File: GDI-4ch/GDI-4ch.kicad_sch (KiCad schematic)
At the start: 312 parts, among them J1 Conn_02x02_Odd_Even, J2 FTSH-107-01-F-DV-K, J3 TC2030, J4 Conn_01x06, J5 Conn_01x04, P1 368255-2, P18 Pad, P19 Pad, P2 Pad, P20 Pad, P3 Pad, P32 Pad, P36 Pad, P4 Pad, P5 Pad, Q1 BUK9230-100B, Q10 BUK9230-100B, Q11 BUK9230-100B, Q12 BUK9230-100B, Q13 AOD4185, Q14 VND14NV04TR-E, Q15 VND14NV04TR-E, Q16 BUK9230-100B, Q2 BUK9230-100B, Q3 BUK9230-100B, Q4 BUK9230-100B, Q5 BUK9230-100B, Q6 BUK9230-100B, Q7 BUK9230-100B, Q8 BUK9230-100B, Q9 BUK9230-100B, U1 MC33816, U2 TJA1051T-3, U3 LM78M05_TO252, U4 74HC14PW,118, U5 XC6206P332MR, U6 MCP6004, U7 GD32F103CBT6, U8 74HC14PW,118, Y1 8MHz, Y2 1MHz

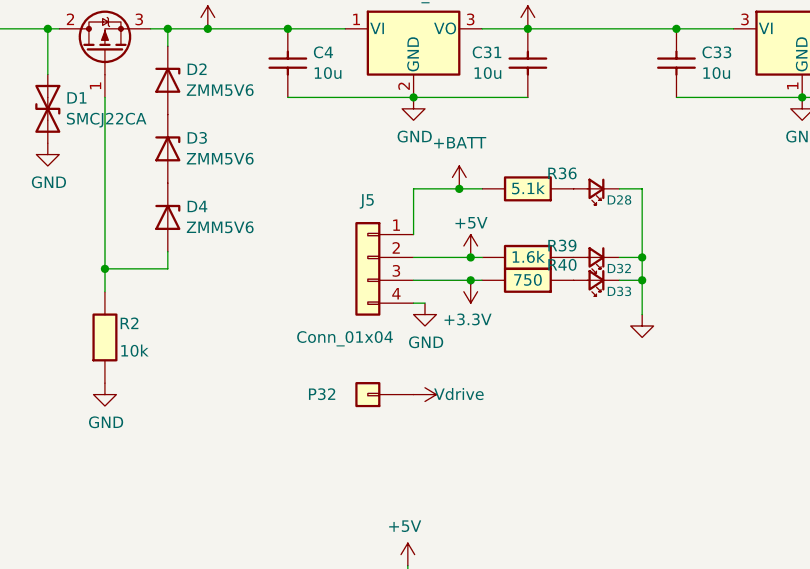
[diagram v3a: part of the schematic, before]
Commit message: 6-pin power connector
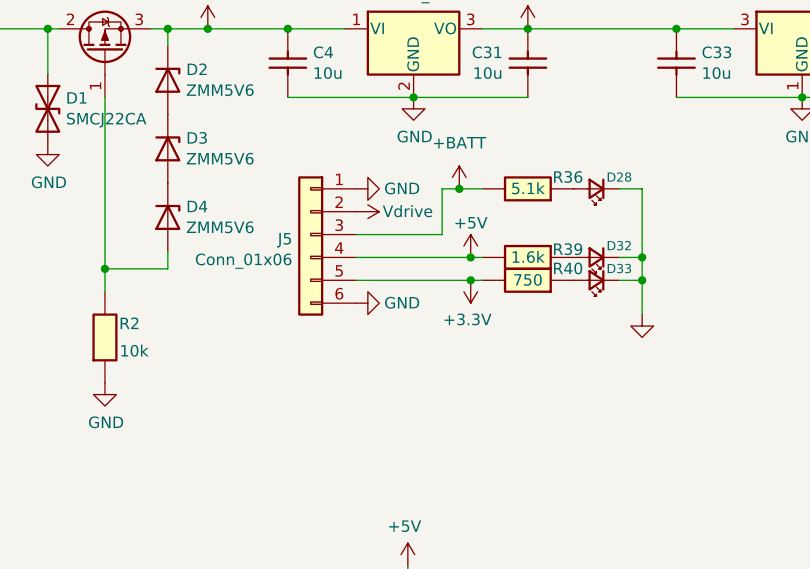
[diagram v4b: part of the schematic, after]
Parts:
- removed J5: Conn_01x04, Connector_PinHeader_2.54mm:PinHeader_1x04_P2.54mm_Vertical, symbol Connector_Generic:Conn_01x04
- removed P32: Pad, hellen-one-common:PAD-TH, symbol hellen-one-common:Pad
- added J5: Conn_01x06, Connector_PinHeader_2.54mm:PinHeader_1x06_P2.54mm_Vertical, symbol Connector_Generic:Conn_01x06
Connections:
- net +3.3V: now also J5.5 (Pin_5)
- net +5V: now also J5.4 (Pin_4)
- net +BATT: now also J5.3 (Pin_3)
- net GND: now also J5.1 (Pin_1), J5.6 (Pin_6)
- net Vdrive: now also J5.2 (Pin_2)
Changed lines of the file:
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@@
     (stroke (width 0) (type default))
   )
+  (wire (pts (xy 113.03 46.99) (xy 122.555 46.99))
+    (stroke (width 0) (type default))
+  )
   (wire (pts (xy 92.075 48.895) (xy 92.075 50.8))
     (stroke (width 0) (type default))
@@
     (stroke (width 0) (type default))
   )
-  (wire (pts (xy 119.38 41.91) (xy 119.38 46.99))
+  (wire (pts (xy 122.555 41.91) (xy 122.555 46.99))
     (stroke (width 0) (type default))
   )
@@
     (stroke (width 0) (type default))
   )
-  (wire (pts (xy 119.38 54.61) (xy 120.65 54.61))
-    (stroke (width 0) (type default))
-  )
   (wire (pts (xy 398.78 104.14) (xy 411.48 104.14))
     (stroke (width 0) (type default))
@@
     (stroke (width 0) (type default))
   )
-  (wire (pts (xy 119.38 49.53) (xy 125.73 49.53))
+  (wire (pts (xy 113.03 49.53) (xy 125.73 49.53))
     (stroke (width 0) (type default))
   )
@@
     (stroke (width 0) (type default))
   )
-  (wire (pts (xy 119.38 41.91) (xy 124.46 41.91))
+  (wire (pts (xy 122.555 41.91) (xy 124.46 41.91))
     (stroke (width 0) (type default))
   )
@@
     (stroke (width 0) (type solid))
   )
-  (wire (pts (xy 119.38 52.07) (xy 125.73 52.07))
+  (wire (pts (xy 113.03 52.07) (xy 125.73 52.07))
     (stroke (width 0) (type default))
   )
@@
   (symbol (lib_id "Device:LED_Small") (at 139.7 49.53 180) (unit 1)
     (in_bom yes) (on_board yes) (dnp no)
-    (property "Reference" "D32" (at 142.24 50.8 0)
+    (property "Reference" "D32" (at 142.24 48.26 0)
       (effects (font (size 1.016 1.016)))
     )
@@
   (symbol (lib_id "Device:LED_Small") (at 139.7 41.91 180) (unit 1)
     (in_bom yes) (on_board yes) (dnp no)
-    (property "Reference" "D28" (at 142.24 43.18 0)
+    (property "Reference" "D28" (at 142.24 40.64 0)
       (effects (font (size 1.016 1.016)))
     )
@@
   (symbol (lib_id "Device:LED_Small") (at 139.7 52.07 180) (unit 1)
     (in_bom yes) (on_board yes) (dnp no)
-    (property "Reference" "D33" (at 142.24 53.34 0)
+    (property "Reference" "D33" (at 142.24 50.8 0)
       (effects (font (size 1.016 1.016)))
     )
@@
   (symbol (lib_id "hellen-one-common:Res") (at 137.16 49.53 180) (unit 1)
     (in_bom yes) (on_board yes) (dnp no)
-    (property "Reference" "R39" (at 135.89 48.26 0)
+    (property "Reference" "R39" (at 136.525 48.6602 0)
       (effects (font (size 1.27 1.27)))
     )
@@
     )
   )
-  (symbol (lib_id "hellen-one-common:Pad") (at 114.3 64.77 180) (unit 1)
-    (in_bom yes) (on_board yes) (dnp no)
-    (property "Reference" "P32" (at 109.22 64.77 0)
-      (effects (font (size 1.27 1.27)))
-    )
-    (property "Value" "Pad" (at 114.3 62.23 0)
-      (effects (font (size 1.27 1.27)) hide)
-    )
-    (property "Footprint" "hellen-one-common:PAD-TH" (at 114.3 60.96 0)
-      (effects (font (size 1.27 1.27)) hide)
-    )
-    (property "Datasheet" "~" (at 114.3 64.77 0)
-      (effects (font (size 1.27 1.27)) hide)
-    )
-    (pin "1")
-    (instances
-      (project "GDI-4ch"
-        (path "/03caada9-9e22-4e2d-9035-b15433dfbb17"
-          (reference "P32") (unit 1)
-        )
-      )
-    )
-  )
   (symbol (lib_id "hellen-one-common:Button_SPST") (at 340.995 16.51 0) (mirror y) (unit 1)
     (in_bom yes) (on_board yes) (dnp no)
@@
     )
   )
-  (symbol (lib_id "Connector_Generic:Conn_01x04") (at 114.3 49.53 0) (mirror y) (unit 1)
-    (in_bom yes) (on_board yes) (dnp no)
-    (property "Reference" "J5" (at 114.3 43.18 0)
-      (effects (font (size 1.27 1.27)))
-    )
-    (property "Value" "Conn_01x04" (at 111.76 58.42 0)
-      (effects (font (size 1.27 1.27)))
-    )
-    (property "Footprint" "Connector_PinHeader_2.54mm:PinHeader_1x04_P2.54mm_Vertical" (at 114.3 49.53 0)
-      (effects (font (size 1.27 1.27)) hide)
-    )
-    (property "Datasheet" "~" (at 114.3 49.53 0)
-      (effects (font (size 1.27 1.27)) hide)
-    )
-    (pin "1")
-    (pin "2")
-    (pin "3")
-    (pin "4")
-    (instances
-      (project "GDI-4ch"
-        (path "/03caada9-9e22-4e2d-9035-b15433dfbb17"
-          (reference "J5") (unit 1)
-        )
-      )
-    )
-  )
   (symbol (lib_id "power:+3.3V") (at 136.525 198.755 0) (unit 1)
     (in_bom yes) (on_board yes) (dnp no)
@@
     )
   )
+  (symbol (lib_id "power:GND") (at 113.03 41.91 90) (unit 1)
+    (in_bom yes) (on_board yes) (dnp no)
+    (property "Reference" "#PWR0150" (at 119.38 41.91 0)
+      (effects (font (size 1.27 1.27)) hide)
+    )
+    (property "Value" "GND" (at 118.11 41.91 90)
+      (effects (font (size 1.27 1.27)))
+    )
+    (property "Footprint" "" (at 113.03 41.91 0)
+      (effects (font (size 1.27 1.27)) hide)
+    )
+    (property "Datasheet" "" (at 113.03 41.91 0)
+      (effects (font (size 1.27 1.27)) hide)
+    )
+    (pin "1")
+    (instances
+      (project "GDI-4ch"
+        (path "/03caada9-9e22-4e2d-9035-b15433dfbb17"
+          (reference "#PWR0150") (unit 1)
+        )
+      )
+    )
+  )
   (symbol (lib_id "Device:R") (at 361.95 66.04 270) (unit 1)
     (in_bom yes) (on_board yes) (dnp no)
@@
     )
   )
-  (symbol (lib_id "power:Vdrive") (at 119.38 64.77 270) (unit 1)
+  (symbol (lib_id "power:Vdrive") (at 113.03 44.45 270) (unit 1)
     (in_bom yes) (on_board yes) (dnp no)
-    (property "Reference" "#PWR024" (at 115.57 59.69 0)
+    (property "Reference" "#PWR024" (at 109.22 39.37 0)
       (effects (font (size 1.27 1.27)) hide)
     )
-    (property "Value" "Vdrive" (at 124.46 64.77 90)
+    (property "Value" "Vdrive" (at 118.745 44.45 90)
       (effects (font (size 1.27 1.27)))
     )
-    (property "Footprint" "" (at 119.38 64.77 0)
+    (property "Footprint" "" (at 113.03 44.45 0)
       (effects (font (size 1.27 1.27)) hide)
     )
-    (property "Datasheet" "" (at 119.38 64.77 0)
+    (property "Datasheet" "" (at 113.03 44.45 0)
       (effects (font (size 1.27 1.27)) hide)
     )
@@
     )
   )
+  (symbol (lib_id "Connector_Generic:Conn_01x06") (at 107.95 46.99 0) (mirror y) (unit 1)
+    (in_bom yes) (on_board yes) (dnp no)
+    (property "Reference" "J5" (at 105.9179 47.4991 0)
+      (effects (font (size 1.27 1.27)) (justify left))
+    )
+    (property "Value" "Conn_01x06" (at 105.9179 49.7978 0)
+      (effects (font (size 1.27 1.27)) (justify left))
+    )
+    (property "Footprint" "Connector_PinHeader_2.54mm:PinHeader_1x06_P2.54mm_Vertical" (at 107.95 46.99 0)
+      (effects (font (size 1.27 1.27)) hide)
+    )
+    (property "Datasheet" "~" (at 107.95 46.99 0)
+      (effects (font (size 1.27 1.27)) hide)
+    )
+    (property "LCSC" "C5156615" (at 107.95 46.99 0)
+      (effects (font (size 1.524 1.524)) hide)
+    )
+    (pin "1")
+    (pin "2")
+    (pin "3")
+    (pin "4")
+    (pin "5")
+    (pin "6")
+    (instances
+      (project "GDI-4ch"
+        (path "/03caada9-9e22-4e2d-9035-b15433dfbb17"
+          (reference "J5") (unit 1)
+        )
+      )
+    )
+  )
   (symbol (lib_id "hellen-one-common:Cap") (at 167.005 202.565 270) (mirror x) (unit 1)
     (in_bom yes) (on_board yes) (dnp no)
@@
     )
   )
-  (symbol (lib_id "power:GND") (at 120.65 54.61 0) (unit 1)
-    (in_bom yes) (on_board yes) (dnp no)
-    (property "Reference" "#PWR0142" (at 120.65 60.96 0)
-      (effects (font (size 1.27 1.27)) hide)
-    )
-    (property "Value" "GND" (at 120.777 59.0042 0)
-      (effects (font (size 1.27 1.27)))
-    )
-    (property "Footprint" "" (at 120.65 54.61 0)
-      (effects (font (size 1.27 1.27)) hide)
-    )
-    (property "Datasheet" "" (at 120.65 54.61 0)
-      (effects (font (size 1.27 1.27)) hide)
-    )
-    (pin "1")
-    (instances
-      (project "GDI-4ch"
-        (path "/03caada9-9e22-4e2d-9035-b15433dfbb17"
-          (reference "#PWR0142") (unit 1)
-        )
-      )
-    )
-  )
   (symbol (lib_id "Device:C") (at 353.06 248.92 0) (mirror x) (unit 1)
     (in_bom yes) (on_board yes) (dnp no)
@@
     )
   )
+  (symbol (lib_id "power:GND") (at 113.03 54.61 90) (unit 1)
+    (in_bom yes) (on_board yes) (dnp no)
+    (property "Reference" "#PWR0142" (at 119.38 54.61 0)
+      (effects (font (size 1.27 1.27)) hide)
+    )
+    (property "Value" "GND" (at 118.11 54.61 90)
+      (effects (font (size 1.27 1.27)))
+    )
+    (property "Footprint" "" (at 113.03 54.61 0)
+      (effects (font (size 1.27 1.27)) hide)
+    )
+    (property "Datasheet" "" (at 113.03 54.61 0)
+      (effects (font (size 1.27 1.27)) hide)
+    )
+    (pin "1")
+    (instances
+      (project "GDI-4ch"
+        (path "/03caada9-9e22-4e2d-9035-b15433dfbb17"
+          (reference "#PWR0142") (unit 1)
+        )
+      )
+    )
+  )
   (symbol (lib_id "power:GND") (at 136.525 233.045 0) (unit 1)
     (in_bom yes) (on_board yes) (dnp no)
@@
   (symbol (lib_id "hellen-one-common:Res") (at 137.16 52.07 0) (mirror y) (unit 1)
     (in_bom yes) (on_board yes) (dnp no)
-    (property "Reference" "R40" (at 135.89 50.3998 0)
+    (property "Reference" "R40" (at 136.525 50.8 0)
       (effects (font (size 1.27 1.27)))
     )
@@
   (symbol (lib_id "hellen-one-common:Res") (at 137.16 41.91 0) (mirror y) (unit 1)
     (in_bom yes) (on_board yes) (dnp no)
-    (property "Reference" "R36" (at 135.89 40.2398 0)
+    (property "Reference" "R36" (at 136.525 40.64 0)
       (effects (font (size 1.27 1.27)))
     )

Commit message: #205
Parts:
- P1: LCSC (none) -> C392284
- U1: value MC33816 -> MC33PT2001AE; LCSC (none) -> C729087
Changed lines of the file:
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@@
       (effects (font (size 1.27 1.27)) hide)
     )
+    (property "LCSC" "C392284" (at 25.4 212.09 0)
+      (effects (font (size 1.524 1.524)) hide)
+    )
     (pin "1")
     (pin "114")
@@
       (effects (font (size 1.27 1.27)) hide)
     )
+    (property "LCSC" "C392284" (at 26.67 29.21 0)
+      (effects (font (size 1.524 1.524)) hide)
+    )
     (pin "1")
     (pin "114")
@@
       (effects (font (size 1.524 1.524)))
     )
-    (property "Value" "MC33816" (at 403.86 135.89 0)
+    (property "Value" "MC33PT2001AE" (at 403.86 135.89 0)
       (effects (font (size 1.524 1.524)))
     )
@@
       (effects (font (size 1.524 1.524)) hide)
     )
+    (property "LCSC" "C729087" (at 403.86 212.09 0)
+      (effects (font (size 1.524 1.524)) hide)
+    )

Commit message: #224, #225 re-fab
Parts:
- J4, J5: LCSC C5156615 -> C37208
- S7, S8: LCSC C115357 -> C455280
- U7: value GD32F103CBT6 -> STM32F103CBT6; LCSC C77979 -> C8304
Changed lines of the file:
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@@
       (effects (font (size 1.27 1.27)) hide)
     )
-    (property "LCSC" "C5156615" (at 551.18 121.92 0)
+    (property "LCSC" "C37208" (at 551.18 121.92 0)
       (effects (font (size 1.524 1.524)) hide)
     )
@@
       (effects (font (size 1.27 1.27)) hide)
     )
-    (property "LCSC" "C115357" (at 340.995 16.51 0)
+    (property "LCSC" "C455280" (at 340.995 16.51 0)
       (effects (font (size 1.27 1.27)) hide)
     )
@@
       (effects (font (size 1.27 1.27)) hide)
     )
-    (property "LCSC" "C115357" (at 341.63 35.56 0)
+    (property "LCSC" "C455280" (at 341.63 35.56 0)
       (effects (font (size 1.27 1.27)) hide)
     )
@@
       (effects (font (size 1.27 1.27)) hide)
     )
-    (property "LCSC" "C5156615" (at 107.95 46.99 0)
+    (property "LCSC" "C37208" (at 107.95 46.99 0)
       (effects (font (size 1.524 1.524)) hide)
     )
@@
       (effects (font (size 1.27 1.27)))
     )
-    (property "Value" "GD32F103CBT6" (at 382.27 118.872 0)
+    (property "Value" "STM32F103CBT6" (at 382.27 118.872 0)
       (effects (font (size 1.27 1.27)))
     )
@@
       (effects (font (size 1.27 1.27)) hide)
     )
-    (property "LCSC" "C77979" (at 383.54 76.2 0)
+    (property "LCSC" "C8304" (at 383.54 76.2 0)
       (effects (font (size 1.524 1.524)) hide)
     )
